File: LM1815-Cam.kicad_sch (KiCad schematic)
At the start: 13 parts, among them IC2A1 LM1815MX_NOPB

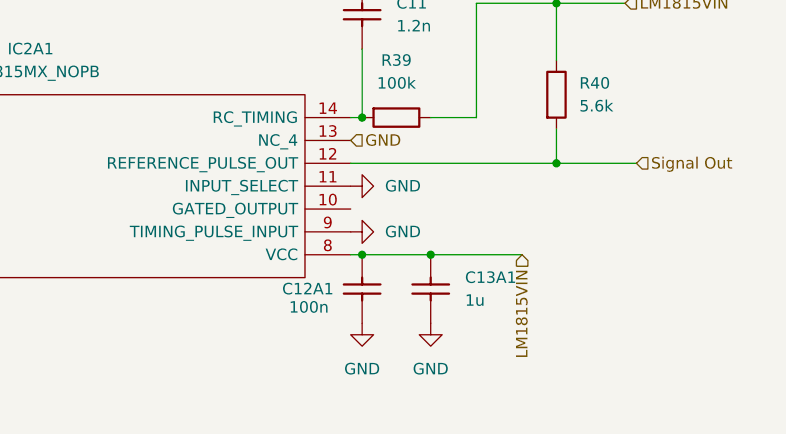
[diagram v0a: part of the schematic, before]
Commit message: Missed two designators
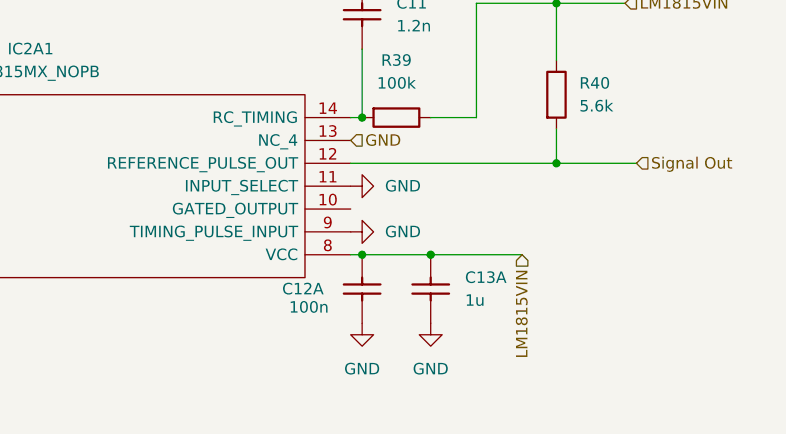
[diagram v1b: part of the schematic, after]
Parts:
- renumbered C12A1 to C12A, C13A1 to C13A
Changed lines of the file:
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@@
 		(on_board yes)
 		(dnp no)
-		(property "Reference" "C12A1"
+		(property "Reference" "C12A"
 			(at 139.7 73.66 90)
 			(effects
@@
 			(project "VFRECU-VR"
 				(path "/90b72e19-92bc-40db-bd4d-f17fb5de93ea/6c826ae6-85e5-4f50-9882-510a117c9583"
-					(reference "C12A1")
+					(reference "C12A")
 					(unit 1)
 				)
@@
 		(dnp no)
 		(fields_autoplaced yes)
-		(property "Reference" "C13A1"
+		(property "Reference" "C13A"
 			(at 160.02 72.3899 90)
 			(effects
@@
 			(project "VFRECU-VR"
 				(path "/90b72e19-92bc-40db-bd4d-f17fb5de93ea/6c826ae6-85e5-4f50-9882-510a117c9583"
-					(reference "C13A1")
-					(unit 1)
-				)
+					(reference "C13A")
+					(unit 1)
+				)

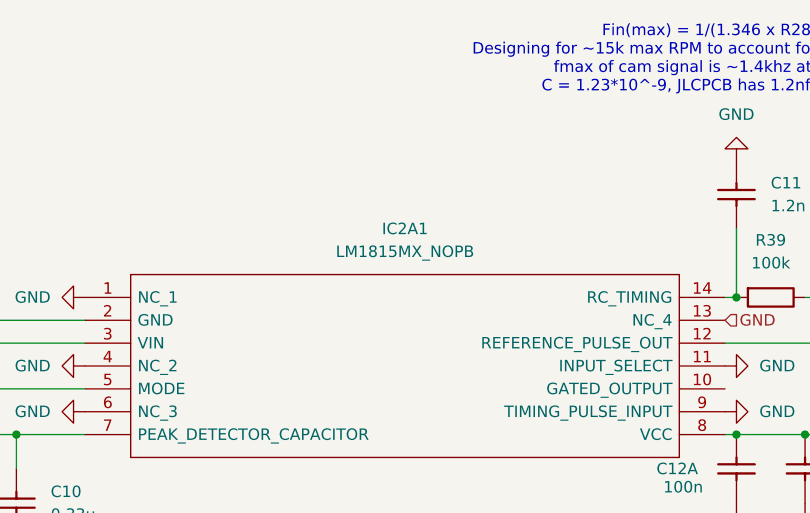
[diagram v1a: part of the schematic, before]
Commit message: Edited designator instead of label
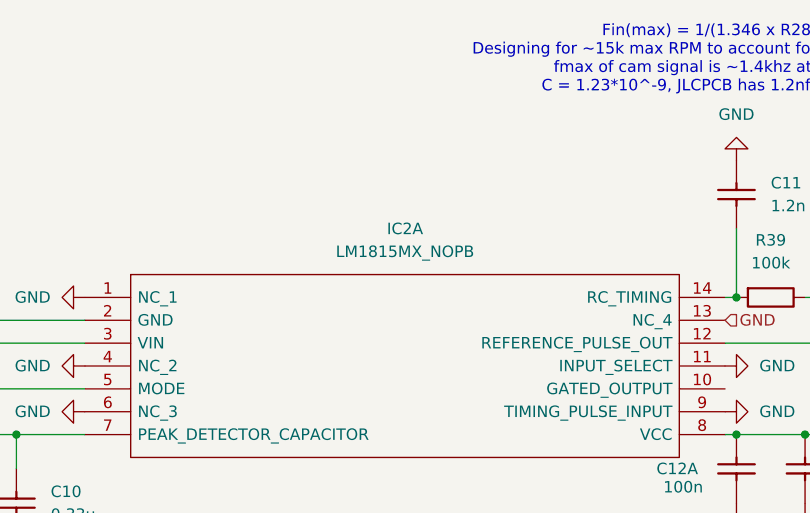
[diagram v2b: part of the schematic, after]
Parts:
- renumbered IC2A1 to IC2A
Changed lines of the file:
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@@
 		(dnp no)
 		(fields_autoplaced yes)
-		(property "Reference" "IC2A1"
+		(property "Reference" "IC2A"
 			(at 111.76 46.99 0)
 			(effects
@@
 			(project "VFRECU-VR"
 				(path "/90b72e19-92bc-40db-bd4d-f17fb5de93ea/6c826ae6-85e5-4f50-9882-510a117c9583"
-					(reference "IC2A1")
+					(reference "IC2A")
 					(unit 1)
 				)

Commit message: More routing changes
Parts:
- renumbered C12A to C12A1, C13A to C13A1, IC2A to IC2A1, R1A to R1A1
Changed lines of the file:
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@@
 		(on_board yes)
 		(dnp no)
-		(property "Reference" "C12A"
+		(property "Reference" "C12A1"
 			(at 139.7 73.66 90)
 			(effects
@@
 			(project "VFRECU-VR"
 				(path "/90b72e19-92bc-40db-bd4d-f17fb5de93ea/6c826ae6-85e5-4f50-9882-510a117c9583"
-					(reference "C12A")
+					(reference "C12A1")
 					(unit 1)
 				)
@@
 		(dnp no)
 		(fields_autoplaced yes)
-		(property "Reference" "IC2A"
+		(property "Reference" "IC2A1"
 			(at 111.76 46.99 0)
 			(effects
@@
 			(project "VFRECU-VR"
 				(path "/90b72e19-92bc-40db-bd4d-f17fb5de93ea/6c826ae6-85e5-4f50-9882-510a117c9583"
-					(reference "IC2A")
+					(reference "IC2A1")
 					(unit 1)
 				)
@@
 		(dnp no)
 		(fields_autoplaced yes)
-		(property "Reference" "C13A"
+		(property "Reference" "C13A1"
 			(at 160.02 72.3899 90)
 			(effects
@@
 			(project "VFRECU-VR"
 				(path "/90b72e19-92bc-40db-bd4d-f17fb5de93ea/6c826ae6-85e5-4f50-9882-510a117c9583"
-					(reference "C13A")
+					(reference "C13A1")
 					(unit 1)
 				)
@@
 		(dnp no)
 		(fields_autoplaced yes)
-		(property "Reference" "R1A"
+		(property "Reference" "R1A1"
 			(at 39.37 53.34 90)
 			(effects
@@
 			(project "VFRECU-VR"
 				(path "/90b72e19-92bc-40db-bd4d-f17fb5de93ea/6c826ae6-85e5-4f50-9882-510a117c9583"
-					(reference "R1A")
-					(unit 1)
-				)
+					(reference "R1A1")
+					(unit 1)
+				)

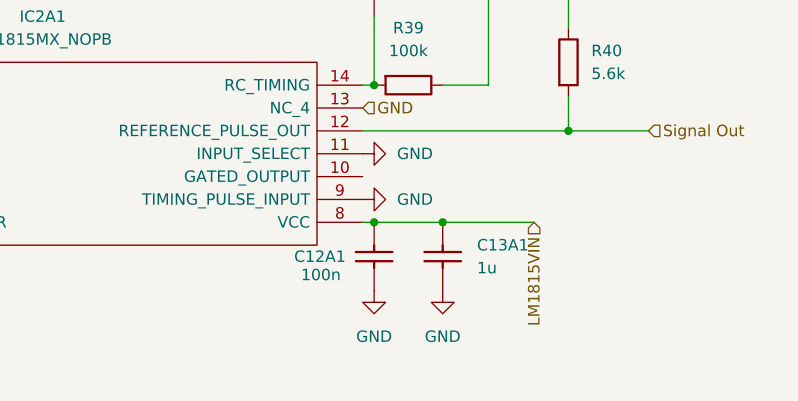
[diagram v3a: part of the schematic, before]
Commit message: Changed component sizes, added stitching vias
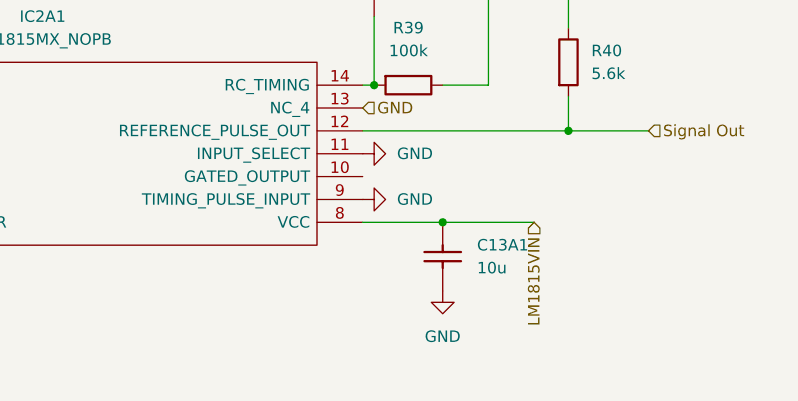
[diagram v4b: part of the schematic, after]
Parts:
- removed C12A1: 100n, Capacitor_SMD:C_0402_1005Metric, symbol hellen-one-common:Cap
- C13A1: value 1u -> 10u; LCSC (none) -> C96446; PN (none) -> CL10A106MA8NRNC
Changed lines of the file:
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@@
-	)
-	(junction
-		(at 148.59 69.85)
-		(diameter 0)
-		(color 0 0 0 0)
 	)
 	(junction
@@
 	(wire
 		(pts
-			(xy 156.21 69.85) (xy 148.59 69.85)
+			(xy 147.32 69.85) (xy 156.21 69.85)
 		)
 		(stroke
@@
 		(pts
 			(xy 33.02 59.69) (xy 35.56 59.69)
-		)
-		(stroke
-			(width 0)
-			(type default)
-		)
-	)
-	(wire
-		(pts
-			(xy 148.59 69.85) (xy 147.32 69.85)
 		)
 		(stroke
@@
 	)
 	(symbol
-		(lib_id "hellen-one-common:Cap")
-		(at 148.59 73.66 90)
-		(unit 1)
-		(exclude_from_sim no)
-		(in_bom yes)
-		(on_board yes)
-		(dnp no)
-		(property "Reference" "C12A1"
-			(at 139.7 73.66 90)
-			(effects
-				(font
-					(size 1.27 1.27)
-				)
-				(justify right)
-			)
-		)
-		(property "Value" "100n"
-			(at 140.462 75.692 90)
-			(effects
-				(font
-					(size 1.27 1.27)
-				)
-				(justify right)
-			)
-		)
-		(property "Footprint" "Capacitor_SMD:C_0402_1005Metric"
-			(at 152.4 76.2 0)
-			(effects
-				(font
-					(size 1.27 1.27)
-				)
-				(hide yes)
-			)
-		)
-		(property "Datasheet" ""
-			(at 148.59 77.47 90)
-			(effects
-				(font
-					(size 1.27 1.27)
-				)
-				(hide yes)
-			)
-		)
-		(property "Description" "Capacitor"
-			(at 148.59 73.66 0)
-			(effects
-				(font
-					(size 1.27 1.27)
-				)
-				(hide yes)
-			)
-		)
-		(property "LCSC" ""
-			(at 148.59 73.66 0)
-			(effects
-				(font
-					(size 1.27 1.27)
-				)
-				(hide yes)
-			)
-		)
-		(pin "2"
-		)
-		(pin "1"
-		)
-		(instances
-			(project "VFRECU-VR"
-				(path "/90b72e19-92bc-40db-bd4d-f17fb5de93ea/6c826ae6-85e5-4f50-9882-510a117c9583"
-					(reference "C12A1")
-					(unit 1)
-				)
-			)
-		)
-	)
-	(symbol
 		(lib_id "power:GND")
 		(at 147.32 67.31 90)
@@
 			)
 		)
-		(property "Value" "1u"
+		(property "Value" "10u"
 			(at 160.02 74.9299 90)
 			(effects
@@
 			)
 		)
-		(property "LCSC" ""
+		(property "LCSC" "C96446"
 			(at 156.21 73.66 0)
+			(effects
+				(font
+					(size 1.27 1.27)
+				)
+				(hide yes)
+			)
+		)
+		(property "PN" "CL10A106MA8NRNC"
+			(at 156.21 73.66 90)
 			(effects
 				(font
@@
 					(unit 1)
 				)
-			)
-		)
-	)
-	(symbol
-		(lib_id "power:GND")
-		(at 148.59 77.47 0)
-		(unit 1)
-		(exclude_from_sim no)
-		(in_bom yes)
-		(on_board yes)
-		(dnp no)
-		(fields_autoplaced yes)
-		(property "Reference" "#PWR098"
-			(at 148.59 83.82 0)
-			(effects
-				(font
-					(size 1.27 1.27)
-				)
-				(hide yes)
-			)
-		)
-		(property "Value" "GND"
-			(at 148.59 82.55 0)
-			(effects
-				(font
-					(size 1.27 1.27)
-				)
-			)
-		)
-		(property "Footprint" ""
-			(at 148.59 77.47 0)
-			(effects
-				(font
-					(size 1.27 1.27)
-				)
-				(hide yes)
-			)
-		)
-		(property "Datasheet" ""
-			(at 148.59 77.47 0)
-			(effects
-				(font
-					(size 1.27 1.27)
-				)
-				(hide yes)
-			)
-		)
-		(property "Description" "Power symbol creates a global label with name \"GND\" , ground"
-			(at 148.59 77.47 0)
-			(effects
-				(font
-					(size 1.27 1.27)
-				)
-				(hide yes)
-			)
-		)
-		(pin "1"
-		)
-		(instances
-			(project "VFRECU-VR"
-				(path "/90b72e19-92bc-40db-bd4d-f17fb5de93ea/6c826ae6-85e5-4f50-9882-510a117c9583"
-					(reference "#PWR098")
-					(unit 1)
-				)
